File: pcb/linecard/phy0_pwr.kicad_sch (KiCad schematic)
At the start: 169 parts, among them U10 VSC8512

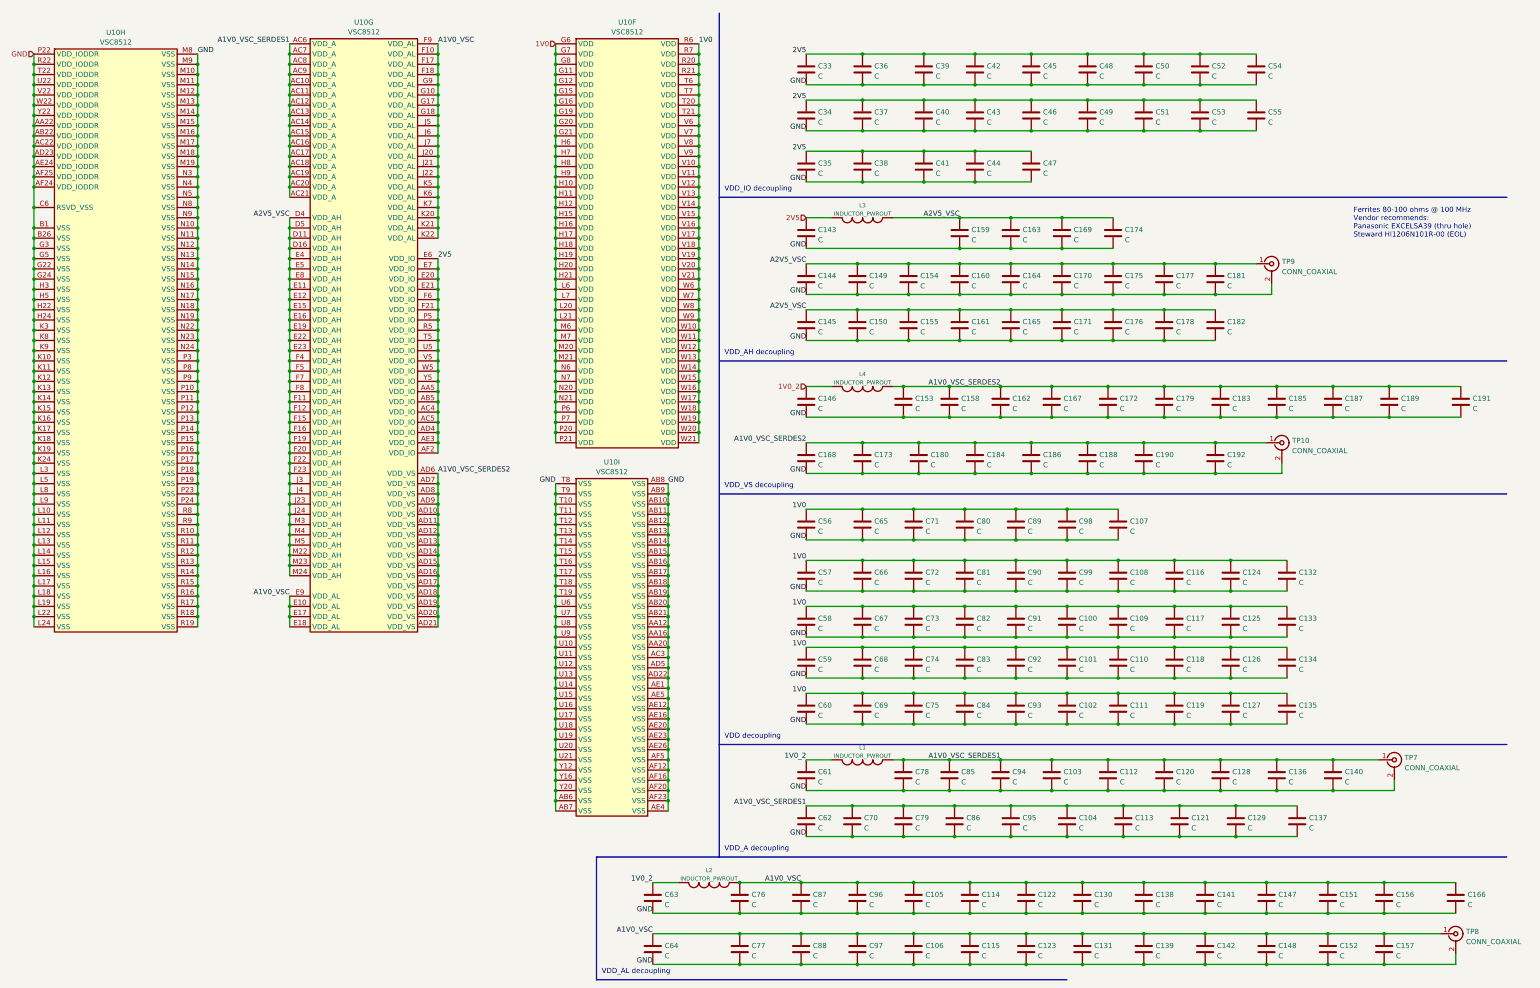
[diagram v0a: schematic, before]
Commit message: Finished initial schematic of line card
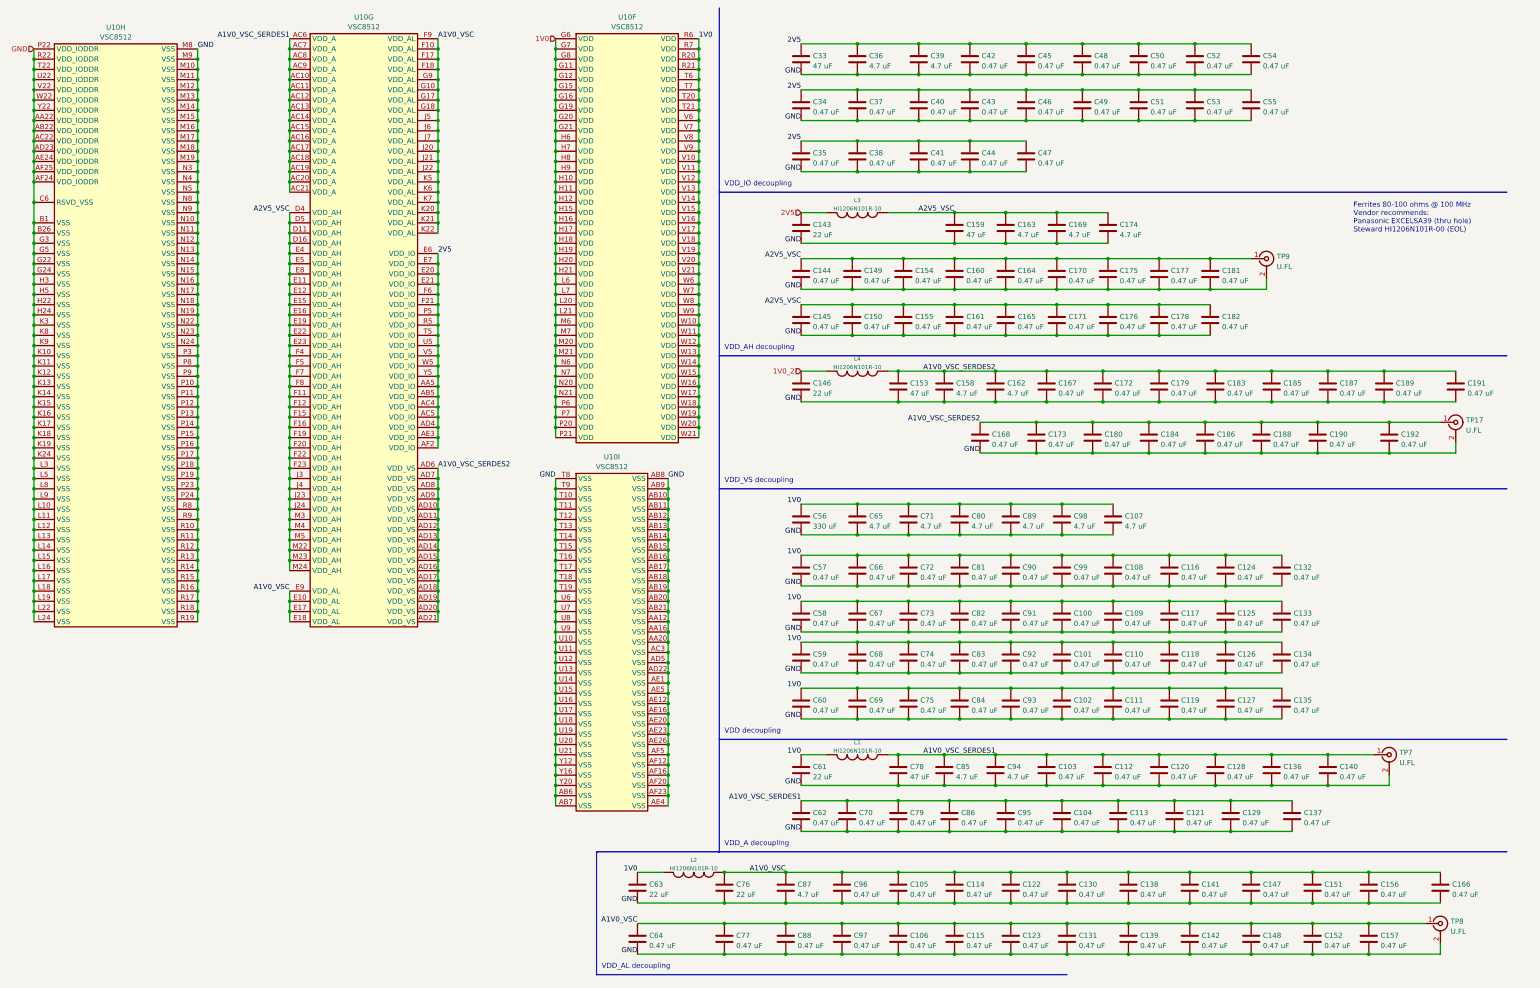
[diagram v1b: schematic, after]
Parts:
- removed TP10: CONN_COAXIAL, azonenberg_pcb:CONN_U.FL_TE_1909763-1, symbol conn:CONN_COAXIAL
- added TP17: U.FL, azonenberg_pcb:CONN_U.FL_TE_1909763-1, symbol conn:CONN_COAXIAL
- C100, C101, C102, C103, C104, C105, C106, C108, C109, C110, C111, C112, C113, C114, C115, C116, C117, C118, C119, C120, C121, C122, C123, C124, C125, C126, C127, C128, C129, C130, C131, C132, C133, C134, C135, C136, C137, C138, C139, C140, C141, C142, C144, C145, C147, C148, C149, C150, C151, C152, C154, C155, C156, C157, C160, C161, C164, C165, C166, C167, C168, C170, C171, C172, C173, C175, C176, C177, C178, C179, C180, C181, C182, C183, C184, C185, C186, C187, C188, C189, C190, C191, C192, C34, C35, C37, C38, C40, C41, C42, C43, C44, C45, C46, C47, C48, C49, C50, C51, C52, C53, C54, C55, C57, C58, C59, C60, C62, C64, C66, C67, C68, C69, C70, C72, C73, C74, C75, C77, C79, C81, C82, C83, C84, C86, C88, C90, C91, C92, C93, C95, C96, C97, C99: value C -> 0.47 uF
- C107, C158, C162, C163, C169, C174, C36, C39, C65, C71, C80, C85, C87, C89, C94, C98: value C -> 4.7 uF
- C143, C146, C61, C63, C76: value C -> 22 uF
- C153, C159, C33, C78: value C -> 47 uF
- C56: value C -> 330 uF
- L1, L2, L3, L4: value INDUCTOR_PWROUT -> HI1206N101R-10
- TP7, TP8, TP9: value CONN_COAXIAL -> U.FL
- U10: footprint (none) -> azonenberg_pcb:BGA_676_27x27_FULLARRAY_1MM_FFG676
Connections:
- net 1V0: now also C61.1, C63.1, L1.2, L2.2
- net 1V0_2: no longer C61.1, C63.1, L1.2, L2.2
- net A1V0_VSC_SERDES2: now also TP17.1 (In)
- net GND: now also TP17.2 (Ext)
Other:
- moved on the sheet: U10F, U10G, U10H, U10I

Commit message: Finished routing of left PHY
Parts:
- C78: footprint azonenberg_pcb:EIA_1206_CAP_NOSILK -> azonenberg_pcb:EIA_1210_CAP_NOSILK
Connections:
- net 1V0: no longer C61.1, C63.1, L1.2, L2.2
- net 1V0_2: now also C61.1, C63.1, L1.2, L2.2
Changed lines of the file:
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@@
 	(title_block
 		(title "LATENTRED Line Card")
-		(date "2024-12-13")
+		(date "2024-12-14")
 		(rev "0.1")
 		(company "Antikernel Labs")
@@
 		)
 	)
-	(label "1V0"
+	(label "1V0_2"
 		(at 191.77 227.33 180)
 		(fields_autoplaced yes)
@@
 		)
 	)
-	(label "1V0"
+	(label "1V0_2"
 		(at 232.41 198.12 180)
 		(fields_autoplaced yes)
@@
 			)
 		)
-		(property "Footprint" "azonenberg_pcb:EIA_1206_CAP_NOSILK"
+		(property "Footprint" "azonenberg_pcb:EIA_1210_CAP_NOSILK"
 			(at 257.5052 205.74 0)
 			(effects
